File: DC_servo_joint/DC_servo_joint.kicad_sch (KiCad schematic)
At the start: 55 parts, among them U1 AS5600, U2 ESP32-C3-WROOM-02, U3 SP3485EN, U5 TPS563200

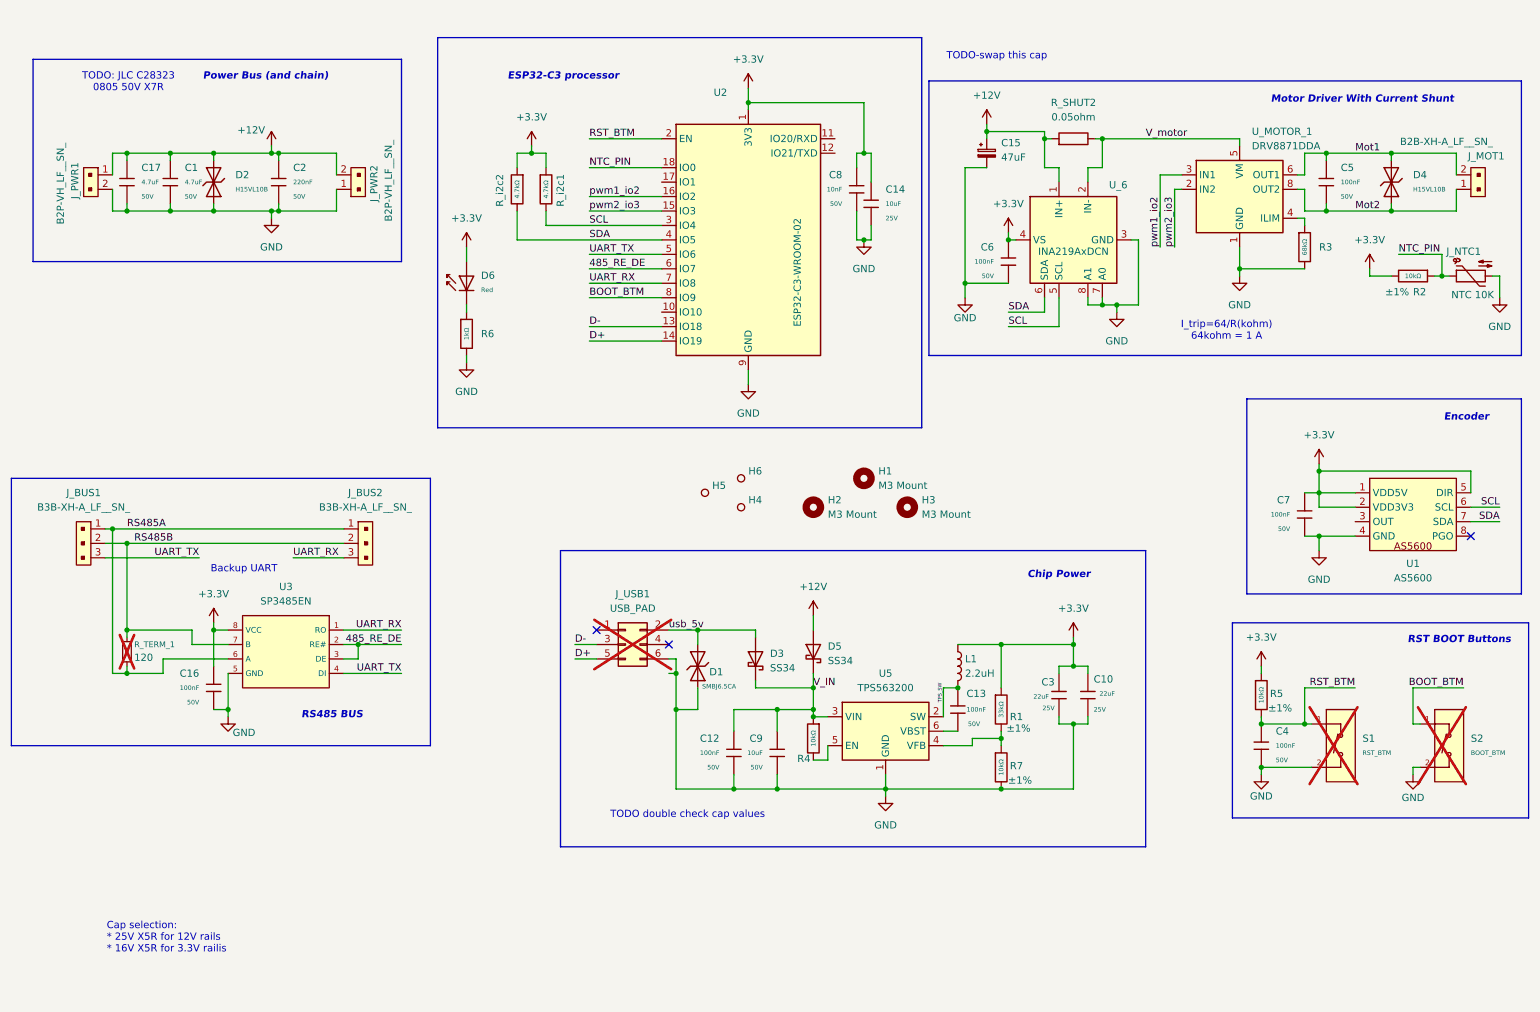
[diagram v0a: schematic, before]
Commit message: Redo details caused by ambiguity,Redirect GPIO2
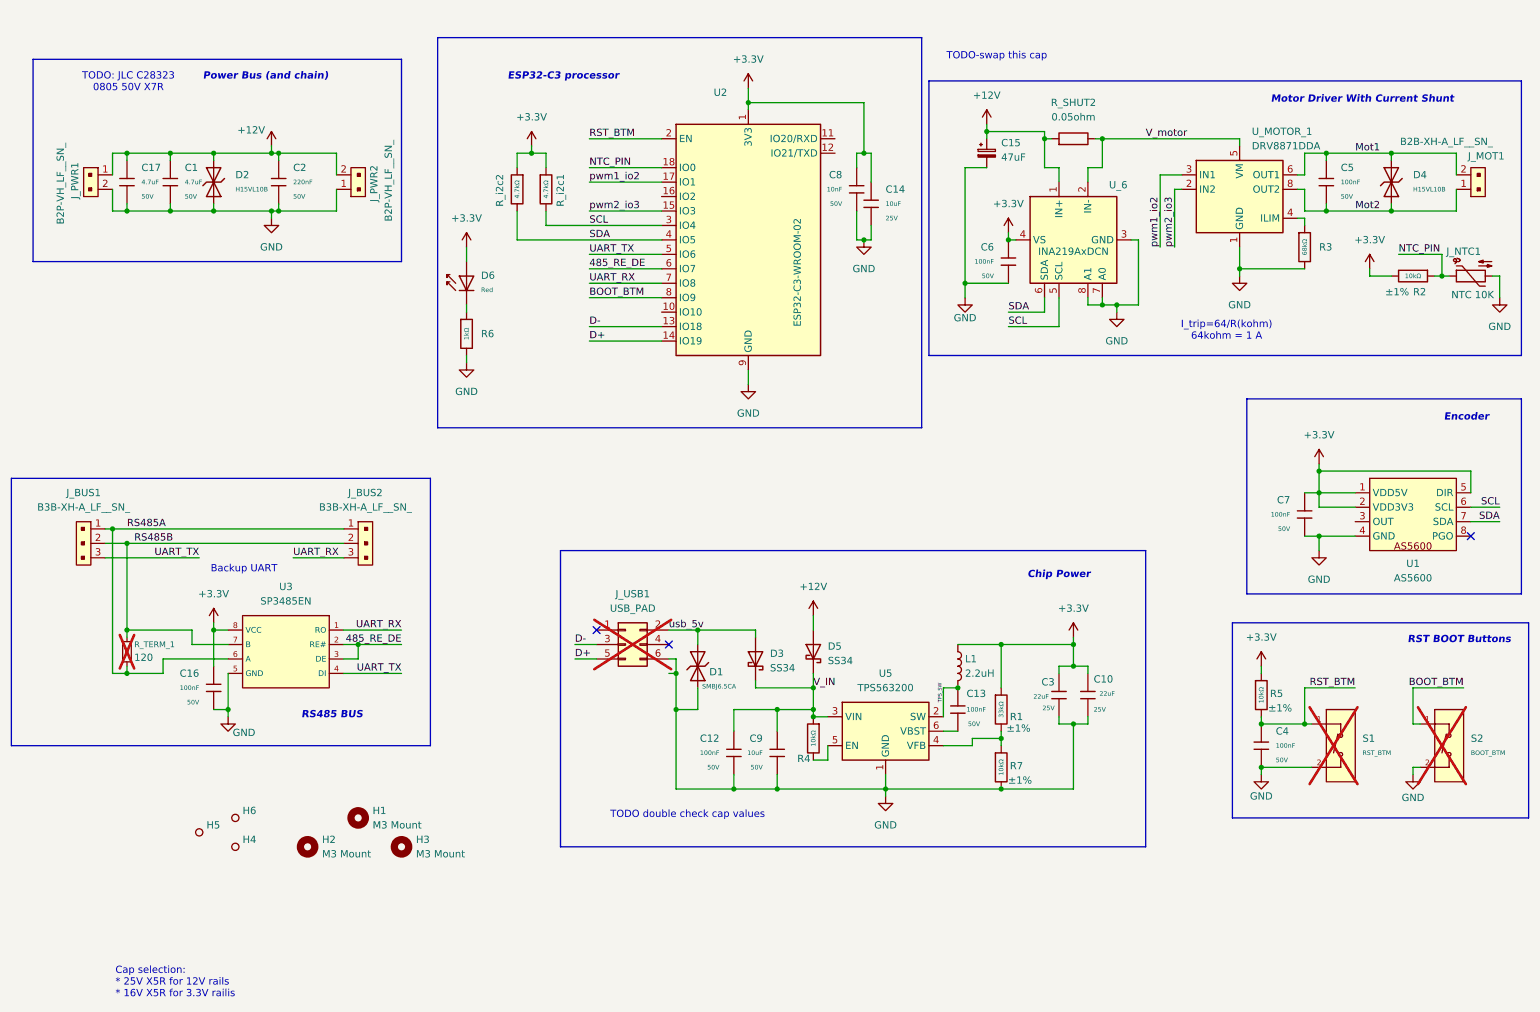
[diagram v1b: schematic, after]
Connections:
- net pwm1_io2: now also U2.17 (IO1); no longer U2.16 (IO2)
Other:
- moved on the sheet: H1, H2, H3, H4, H5, H6
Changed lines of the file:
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@@
 	(text "Cap selection:\n* 25V X5R for 12V rails\n* 16V X5R for 3.3V railis"
 		(exclude_from_sim no)
-		(at 29.464 177.292 0)
+		(at 30.988 185.166 0)
 		(effects
 			(font
@@
 	(wire
 		(pts
+			(xy 114.3 44.45) (xy 127 44.45)
+		)
+		(stroke
+			(width 0)
+			(type default)
+		)
+	)
+	(wire
+		(pts
 			(xy 92.71 66.04) (xy 92.71 67.31)
 		)
@@
 	(wire
 		(pts
-			(xy 114.3 46.99) (xy 127 46.99)
-		)
-		(stroke
-			(width 0)
-			(type default)
-		)
-	)
-	(wire
-		(pts
 			(xy 243.84 48.26) (xy 243.84 49.53)
 		)
@@
 		)
 	)
-	(label "pwm1_io2"
-		(at 114.3 46.99 0)
-		(effects
-			(font
-				(size 1.27 1.27)
-			)
-			(justify left bottom)
-		)
-	)
 	(label "Mot1"
 		(at 248.92 39.37 0)
@@
 		)
 	)
+	(label "pwm1_io2"
+		(at 114.3 44.45 0)
+		(effects
+			(font
+				(size 1.27 1.27)
+			)
+			(justify left bottom)
+		)
+	)
 	(label "RS485A"
 		(at 33.02 105.41 0)
@@
 	(symbol
 		(lib_id "Mechanical:MountingHole")
-		(at 162.56 96.52 0)
+		(at 73.66 156.21 0)
 		(unit 1)
 		(exclude_from_sim no)
@@
 		(fields_autoplaced yes)
 		(property "Reference" "H1"
-			(at 165.1 95.2499 0)
+			(at 76.2 154.9399 0)
 			(effects
 				(font
@@
 		)
 		(property "Value" "M3 Mount"
-			(at 165.1 97.7899 0)
+			(at 76.2 157.4799 0)
 			(effects
 				(font
@@
 		)
 		(property "Footprint" "MountingHole:MountingHole_3.2mm_M3_DIN965"
-			(at 162.56 96.52 0)
+			(at 73.66 156.21 0)
 			(effects
 				(font
@@
 		)
 		(property "Datasheet" "~"
-			(at 162.56 96.52 0)
+			(at 73.66 156.21 0)
 			(effects
 				(font
@@
 		)
 		(property "Description" "Mounting Hole without connection"
-			(at 162.56 96.52 0)
+			(at 73.66 156.21 0)
 			(effects
 				(font
@@
 	(symbol
 		(lib_id "PCM_JLCPCB-Manufacturing:Tooling Hole, PCM_JLCPCB, 1.152mm")
-		(at 134.62 99.06 0)
+		(at 45.72 158.75 0)
 		(unit 1)
 		(exclude_from_sim no)
@@
 		(fields_autoplaced yes)
 		(property "Reference" "H5"
-			(at 135.89 97.7899 0)
+			(at 46.99 157.4799 0)
 			(effects
 				(font
@@
 		)
 		(property "Value" "~"
-			(at 135.89 100.3299 0)
+			(at 46.99 160.0199 0)
 			(effects
 				(font
@@
 		)
 		(property "Footprint" "PCM_JLCPCB:Hole_Tooling_JLCPCB"
-			(at 134.62 99.06 0)
+			(at 45.72 158.75 0)
 			(effects
 				(font
@@
 		)
 		(property "Datasheet" "https://jlcpcb.com/help/article/How-to-add-tooling-holes-for-PCB-assembly-order"
-			(at 134.62 99.06 0)
+			(at 45.72 158.75 0)
 			(effects
 				(font
@@
 		)
 		(property "Description" "1. Two or three tooling holes should be added on the PCB, they should be placed in opposite corners of the PCB and as far apart from one another as practical. 2. Tooling holes should be 1.152mm(45.4mil) round non-plated holes with 0.148mm solder mask expansion. 3. Tooling holes are only required for PCB assembly orders. 4. Please try to add tooling holes on empty space and keep them away from traces. If there is no enough room, you can add them to the copper area."
-			(at 134.62 99.06 0)
+			(at 45.72 158.75 0)
 			(effects
 				(font
@@
 	(symbol
 		(lib_id "Mechanical:MountingHole")
-		(at 153.67 101.6 0)
+		(at 64.77 161.29 0)
 		(unit 1)
 		(exclude_from_sim no)
@@
 		(fields_autoplaced yes)
 		(property "Reference" "H2"
-			(at 156.21 100.3299 0)
+			(at 67.31 160.0199 0)
 			(effects
 				(font
@@
 		)
 		(property "Value" "M3 Mount"
-			(at 156.21 102.8699 0)
+			(at 67.31 162.5599 0)
 			(effects
 				(font
@@
 		)
 		(property "Footprint" "MountingHole:MountingHole_3.2mm_M3_DIN965"
-			(at 153.67 101.6 0)
+			(at 64.77 161.29 0)
 			(effects
 				(font
@@
 		)
 		(property "Datasheet" "~"
-			(at 153.67 101.6 0)
+			(at 64.77 161.29 0)
 			(effects
 				(font
@@
 		)
 		(property "Description" "Mounting Hole without connection"
-			(at 153.67 101.6 0)
+			(at 64.77 161.29 0)
 			(effects
 				(font
@@
 	(symbol
 		(lib_id "PCM_JLCPCB-Manufacturing:Tooling Hole, PCM_JLCPCB, 1.152mm")
-		(at 140.97 101.6 0)
+		(at 52.07 161.29 0)
 		(unit 1)
 		(exclude_from_sim no)
@@
 		(fields_autoplaced yes)
 		(property "Reference" "H4"
-			(at 142.24 100.3299 0)
+			(at 53.34 160.0199 0)
 			(effects
 				(font
@@
 		)
 		(property "Value" "~"
-			(at 142.24 102.8699 0)
+			(at 53.34 162.5599 0)
 			(effects
 				(font
@@
 		)
 		(property "Footprint" "PCM_JLCPCB:Hole_Tooling_JLCPCB"
-			(at 140.97 101.6 0)
+			(at 52.07 161.29 0)
 			(effects
 				(font
@@
 		)
 		(property "Datasheet" "https://jlcpcb.com/help/article/How-to-add-tooling-holes-for-PCB-assembly-order"
-			(at 140.97 101.6 0)
+			(at 52.07 161.29 0)
 			(effects
 				(font
@@
 		)
 		(property "Description" "1. Two or three tooling holes should be added on the PCB, they should be placed in opposite corners of the PCB and as far apart from one another as practical. 2. Tooling holes should be 1.152mm(45.4mil) round non-plated holes with 0.148mm solder mask expansion. 3. Tooling holes are only required for PCB assembly orders. 4. Please try to add tooling holes on empty space and keep them away from traces. If there is no enough room, you can add them to the copper area."
-			(at 140.97 101.6 0)
+			(at 52.07 161.29 0)
 			(effects
 				(font
@@
 	(symbol
 		(lib_id "Mechanical:MountingHole")
-		(at 170.18 101.6 0)
+		(at 81.28 161.29 0)
 		(unit 1)
 		(exclude_from_sim no)
@@
 		(fields_autoplaced yes)
 		(property "Reference" "H3"
-			(at 172.72 100.3299 0)
+			(at 83.82 160.0199 0)
 			(effects
 				(font
@@
 		)
 		(property "Value" "M3 Mount"
-			(at 172.72 102.8699 0)
+			(at 83.82 162.5599 0)
 			(effects
 				(font
@@
 		)
 		(property "Footprint" "MountingHole:MountingHole_3.2mm_M3_DIN965"
-			(at 170.18 101.6 0)
+			(at 81.28 161.29 0)
 			(effects
 				(font
@@
 		)
 		(property "Datasheet" "~"
-			(at 170.18 101.6 0)
+			(at 81.28 161.29 0)
 			(effects
 				(font
@@
 		)
 		(property "Description" "Mounting Hole without connection"
-			(at 170.18 101.6 0)
+			(at 81.28 161.29 0)
 			(effects
 				(font
@@
 	(symbol
 		(lib_id "PCM_JLCPCB-Manufacturing:Tooling Hole, PCM_JLCPCB, 1.152mm")
-		(at 140.97 96.52 0)
+		(at 52.07 156.21 0)
 		(unit 1)
 		(exclude_from_sim no)
@@
 		(fields_autoplaced yes)
 		(property "Reference" "H6"
-			(at 142.24 95.2499 0)
+			(at 53.34 154.9399 0)
 			(effects
 				(font
@@
 		)
 		(property "Value" "~"
-			(at 142.24 97.7899 0)
+			(at 53.34 157.4799 0)
 			(effects
 				(font
@@
 		)
 		(property "Footprint" "PCM_JLCPCB:Hole_Tooling_JLCPCB"
-			(at 140.97 96.52 0)
+			(at 52.07 156.21 0)
 			(effects
 				(font
@@
 		)
 		(property "Datasheet" "https://jlcpcb.com/help/article/How-to-add-tooling-holes-for-PCB-assembly-order"
-			(at 140.97 96.52 0)
+			(at 52.07 156.21 0)
 			(effects
 				(font
@@
 		)
 		(property "Description" "1. Two or three tooling holes should be added on the PCB, they should be placed in opposite corners of the PCB and as far apart from one another as practical. 2. Tooling holes should be 1.152mm(45.4mil) round non-plated holes with 0.148mm solder mask expansion. 3. Tooling holes are only required for PCB assembly orders. 4. Please try to add tooling holes on empty space and keep them away from traces. If there is no enough room, you can add them to the copper area."
-			(at 140.97 96.52 0)
+			(at 52.07 156.21 0)
 			(effects
 				(font

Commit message: Save the final production run of the circuit. mistake on AS5600 pinout
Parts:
- H4, H5, H6: now left out of the parts list
- U3: FT Rotation Offset (none) -> 90
- U_MOTOR_1: FT Rotation Offset (none) -> -90
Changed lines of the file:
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@@
 			)
 		)
+		(property "FT Rotation Offset" "90"
+			(at 60.96 128.27 0)
+			(effects
+				(font
+					(size 1.27 1.27)
+				)
+				(hide yes)
+			)
+		)
 		(pin "6"
 		)
@@
 			)
 		)
+		(property "FT Rotation Offset" "-90"
+			(at 228.6 45.72 0)
+			(effects
+				(font
+					(size 1.27 1.27)
+				)
+				(hide yes)
+			)
+		)
 		(pin "4"
 		)
@@
 		(unit 1)
 		(exclude_from_sim no)
-		(in_bom yes)
+		(in_bom no)
 		(on_board yes)
 		(dnp no)
@@
 		(unit 1)
 		(exclude_from_sim no)
-		(in_bom yes)
+		(in_bom no)
 		(on_board yes)
 		(dnp no)
@@
 		(unit 1)
 		(exclude_from_sim no)
-		(in_bom yes)
+		(in_bom no)
 		(on_board yes)
 		(dnp no)

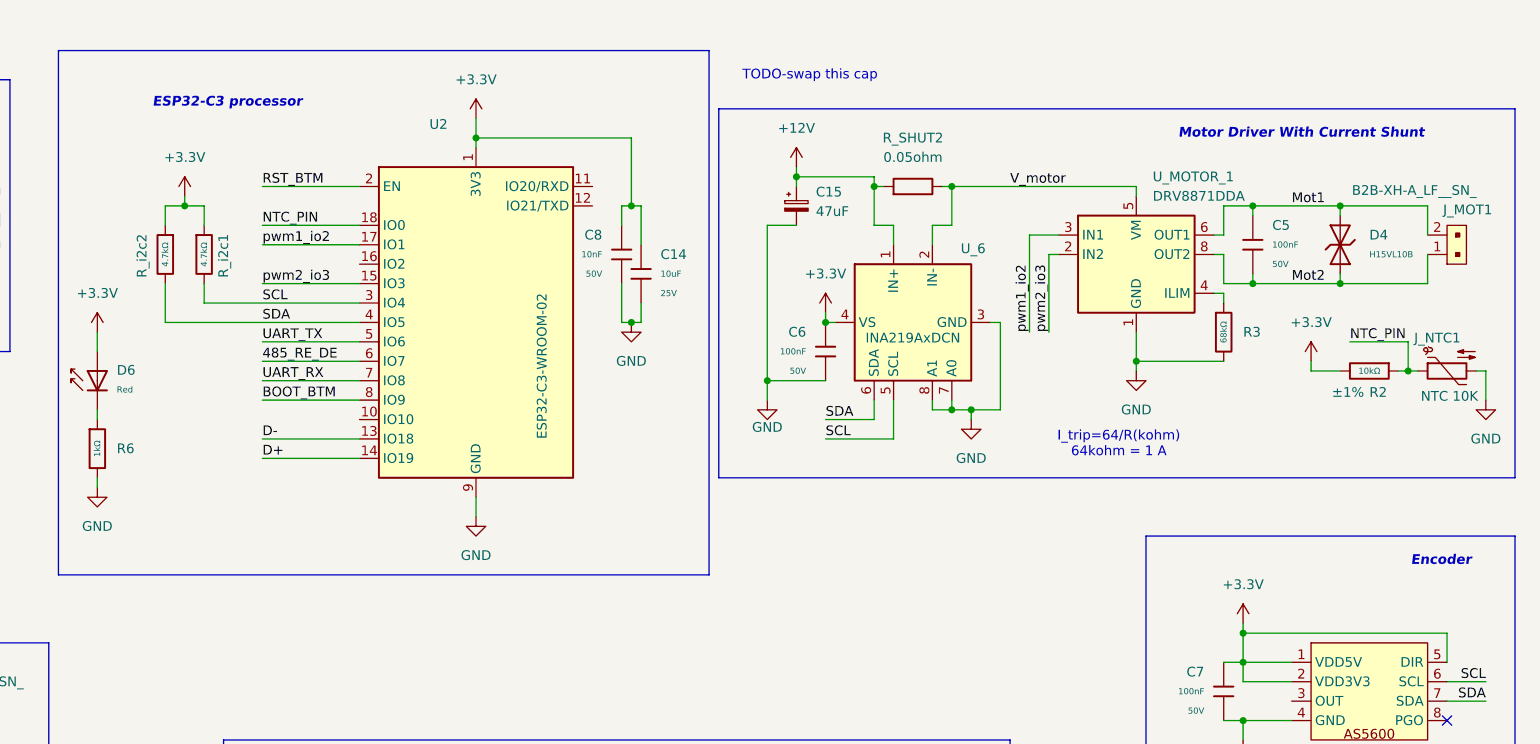
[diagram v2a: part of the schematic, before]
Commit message: Mark out the error on the DC servo joint PCB
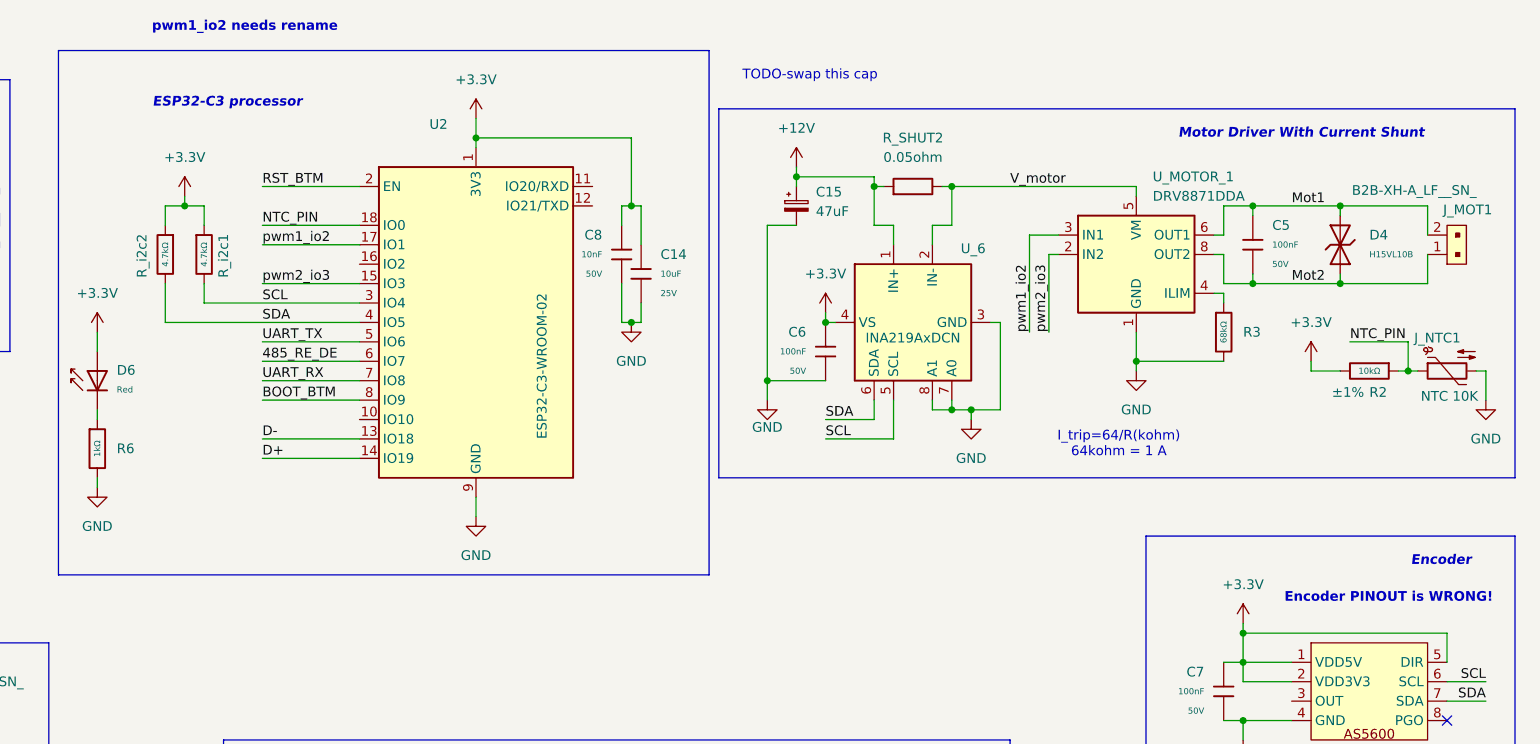
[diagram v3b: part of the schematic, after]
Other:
- note added: "Encoder PINOUT is WRONG!"
- note added: "pwm1_io2 needs rename"
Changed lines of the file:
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@@
+		)
+	)
+	(text "pwm1_io2 needs rename"
+		(exclude_from_sim no)
+		(at 112.014 16.002 0)
+		(effects
+			(font
+				(size 1.27 1.27)
+				(thickness 0.254)
+				(bold yes)
+				(color 194 0 0 1)
+			)
 		)
 	)
@@
 			)
 		)
+	)
+	(text "Encoder PINOUT is WRONG!"
+		(exclude_from_sim no)
+		(at 261.62 90.678 0)
+		(effects
+			(font
+				(size 1.27 1.27)
+				(thickness 0.254)
+				(bold yes)
+				(color 194 0 0 1)
+			)
+		)
